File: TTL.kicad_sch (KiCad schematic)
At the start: 2 parts, among them U6 CH340E

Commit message: Assign footprints to devices
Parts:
- C5: footprint (none) -> Capacitor_SMD:C_0201_0603Metric
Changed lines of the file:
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@@
 			)
 		)
-		(property "Footprint" ""
+		(property "Footprint" "Capacitor_SMD:C_0201_0603Metric"
 			(at 91.1352 48.26 0)
 			(effects

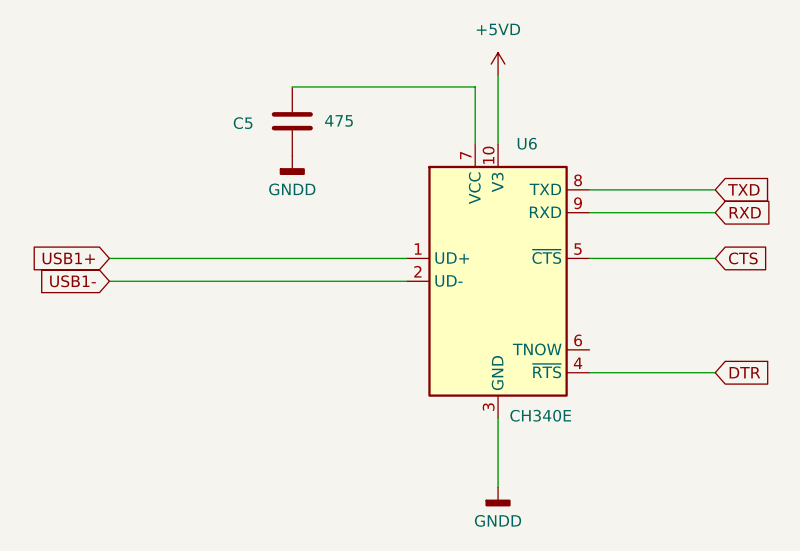
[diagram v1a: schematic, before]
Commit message: Move Radio interface onto it's own sheet, Add mounting holes and case outline
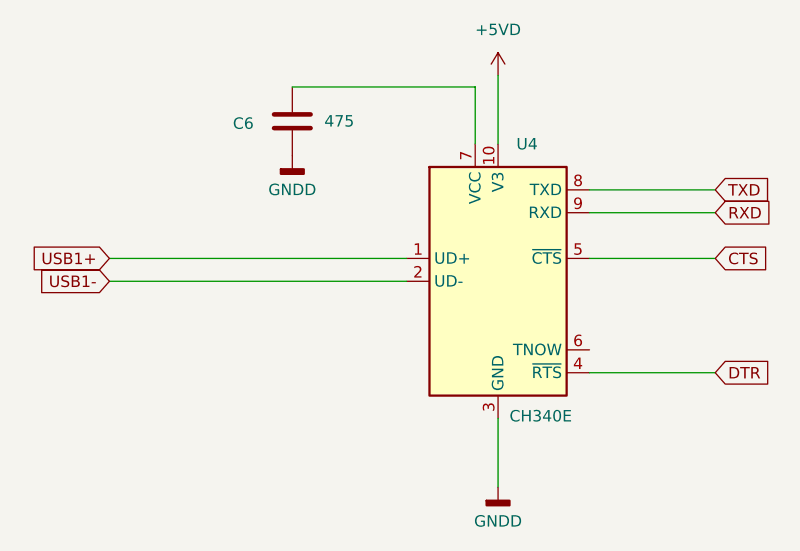
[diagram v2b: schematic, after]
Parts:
- renumbered C5 to C6, U6 to U4
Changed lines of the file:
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@@
 		(on_board yes)
 		(dnp no)
-		(property "Reference" "C5"
+		(property "Reference" "C6"
 			(at 83.566 44.704 0)
 			(effects
@@
 			(project "digital-mode-radio-interface"
 				(path "/a0d4bcf6-6cac-4e92-853e-9083f008b231/74e4e8e2-a92b-448e-a5b4-a60ebc3dca8a"
-					(reference "C5")
+					(reference "C6")
 					(unit 1)
 				)
@@
 		(on_board yes)
 		(dnp no)
-		(property "Reference" "U6"
+		(property "Reference" "U4"
 			(at 115.062 46.99 0)
 			(effects
@@
 			(project "digital-mode-radio-interface"
 				(path "/a0d4bcf6-6cac-4e92-853e-9083f008b231/74e4e8e2-a92b-448e-a5b4-a60ebc3dca8a"
-					(reference "U6")
+					(reference "U4")
 					(unit 1)
 				)
